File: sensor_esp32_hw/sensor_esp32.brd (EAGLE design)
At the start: 58.5 x 25.5 mm, 31 parts, among them IC1 ESP32-C3-WROOM-02-N4, IC2 ESP32-WROOM-32UE-N16, Q1 DMG3415, U1 AHT20, U2 TPL5110

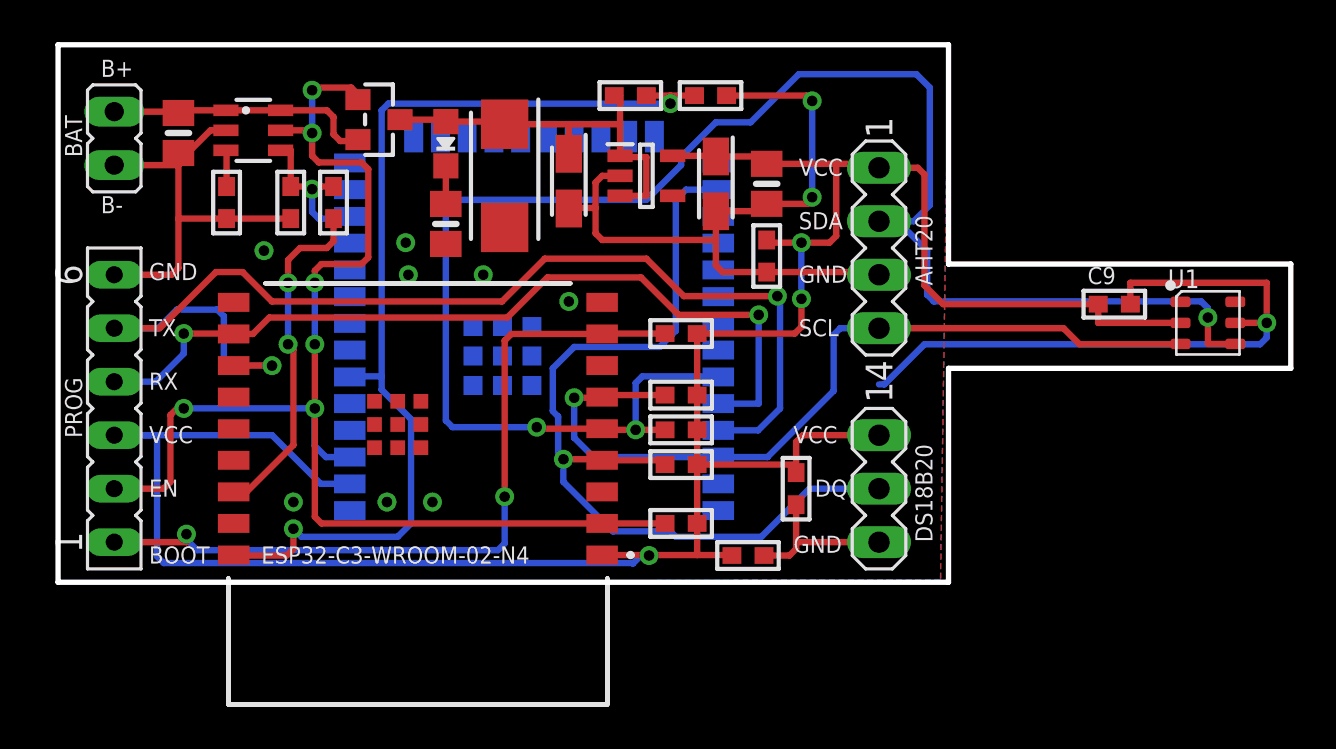
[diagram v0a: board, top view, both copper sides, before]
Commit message: added another esp32 with u.fl connection (if needed)
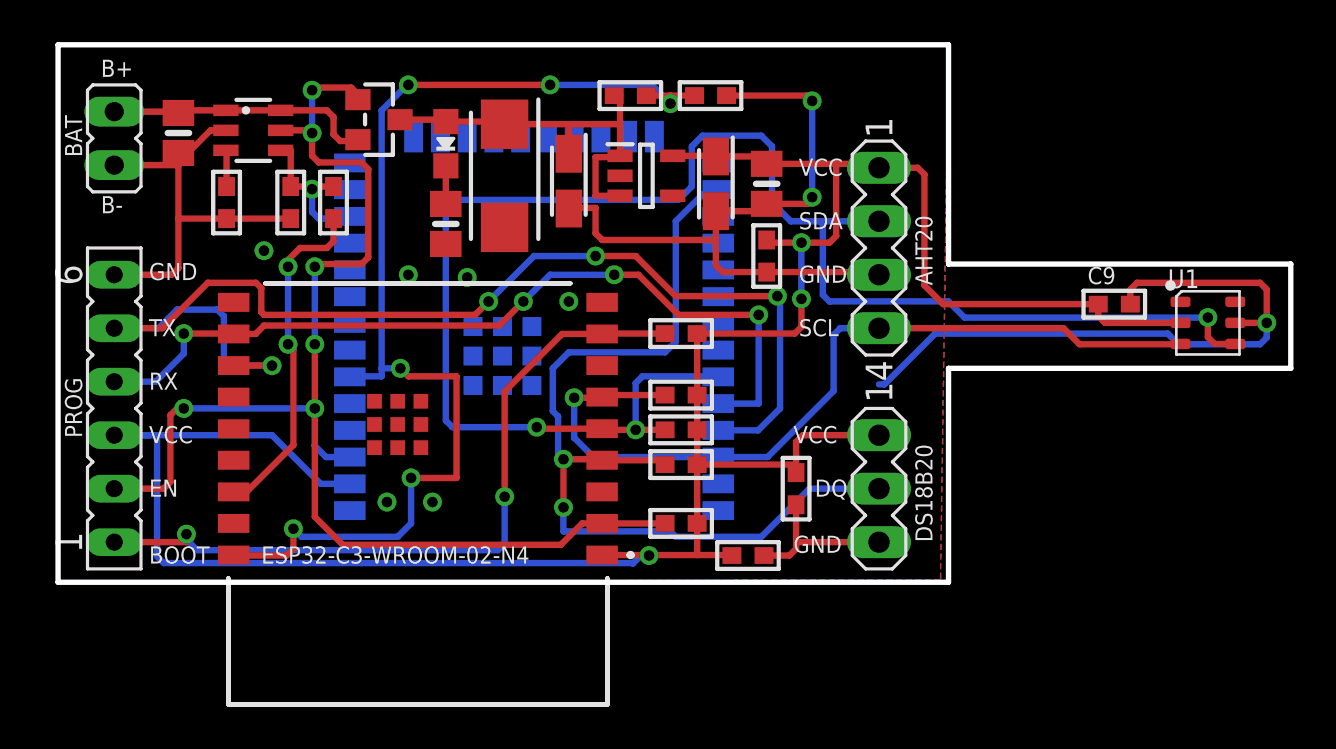
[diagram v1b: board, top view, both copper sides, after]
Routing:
- net PWROUT_DIV: track 48.2 -> 54.2 mm, vias 2 -> 6
- net SDA: track 83.3 -> 79.2 mm
- net GND: track 93.9 -> 91.4 mm, vias 11 -> 9
- net BOOT: track 36.9 -> 35.5 mm
- net EN: track 62.4 -> 63.6 mm
- net DQ: track 42.7 -> 43.8 mm, vias 1 -> 2
- net TXD0: track 55.5 -> 56.4 mm, vias 2 -> 4
- net RXD0: track 40.1 -> 40.2 mm, vias 2 -> 4

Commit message: minor routing improvements
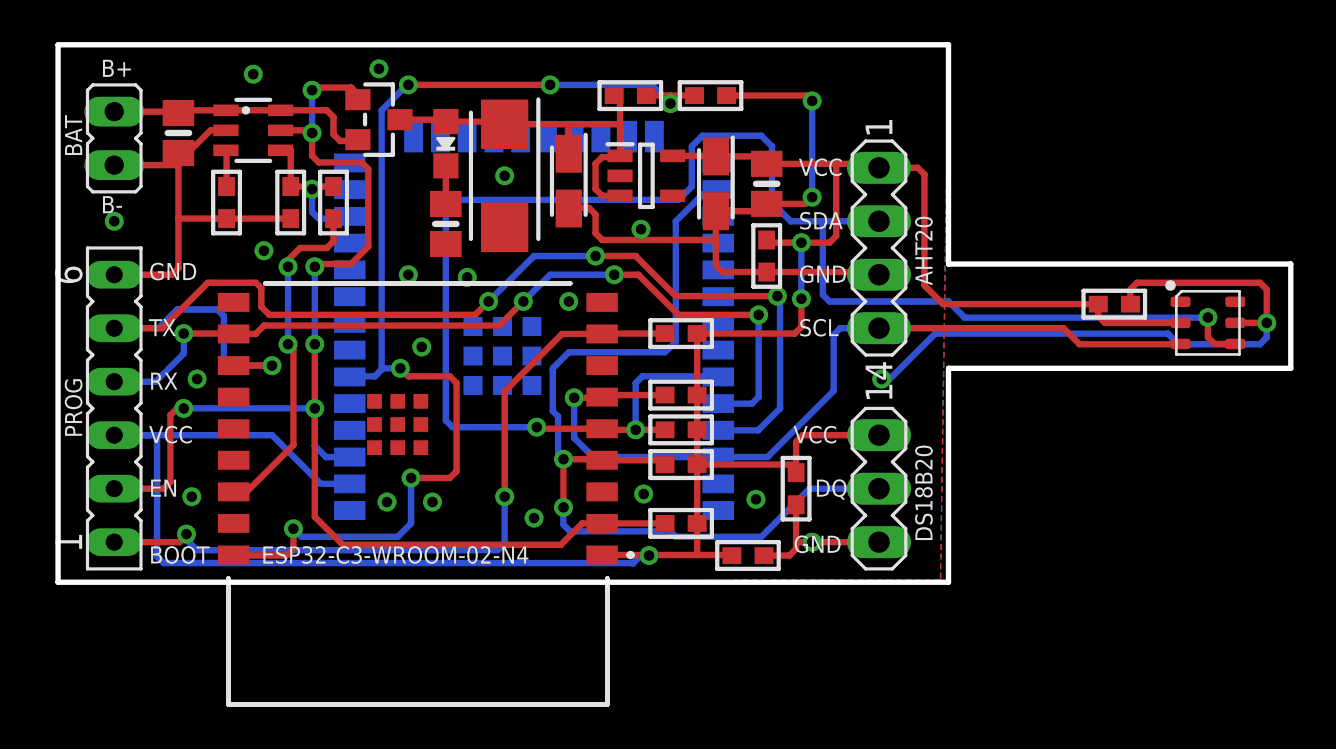
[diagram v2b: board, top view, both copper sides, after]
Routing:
- net PWROUT_DIV: track 54.2 -> 53.7 mm
- net GND: track 91.4 -> 91.1 mm, vias 9 -> 22

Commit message: minor improvements before fabrication
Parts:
- added C10, C11: 100 nF, microbuilder:_0603
- C3: value 22 uF -> 10 uF
- PS1: value AP2202K-3.3TRG1 -> LDI8119-3.3EN-DIO
- moved C2 8.81 mm to (29.5, 18.3)
- moved C4 8.64 mm to (38.6, 22.4), turned to 0 degrees
- moved R11 2.96 mm to (33.4, 22.5)
- moved C3 2.16 mm to (21.6, 18.9)
- moved PS1 2.16 mm to (25.3, 19.2)
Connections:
- net GND: now also C10.2, C11.2
- net N$1: now also IC1.15; no longer IC1.16
- net PWROUT: now also C11.1; no longer C2.1
- net PWROUT_DIV: now also C10.1
- net VCC: now also C2.1
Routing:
- net GND: track 91.1 -> 80.9 mm, vias 22 -> 23
- net VCC: track 117.9 -> 123.5 mm
- net PWROUT_DIV: track 53.7 -> 58.3 mm
- net N$1: track 16.3 -> 15.0 mm
- net TXD0: track 56.2 -> 55.2 mm
- net PWROUT: track 19.1 -> 20.1 mm

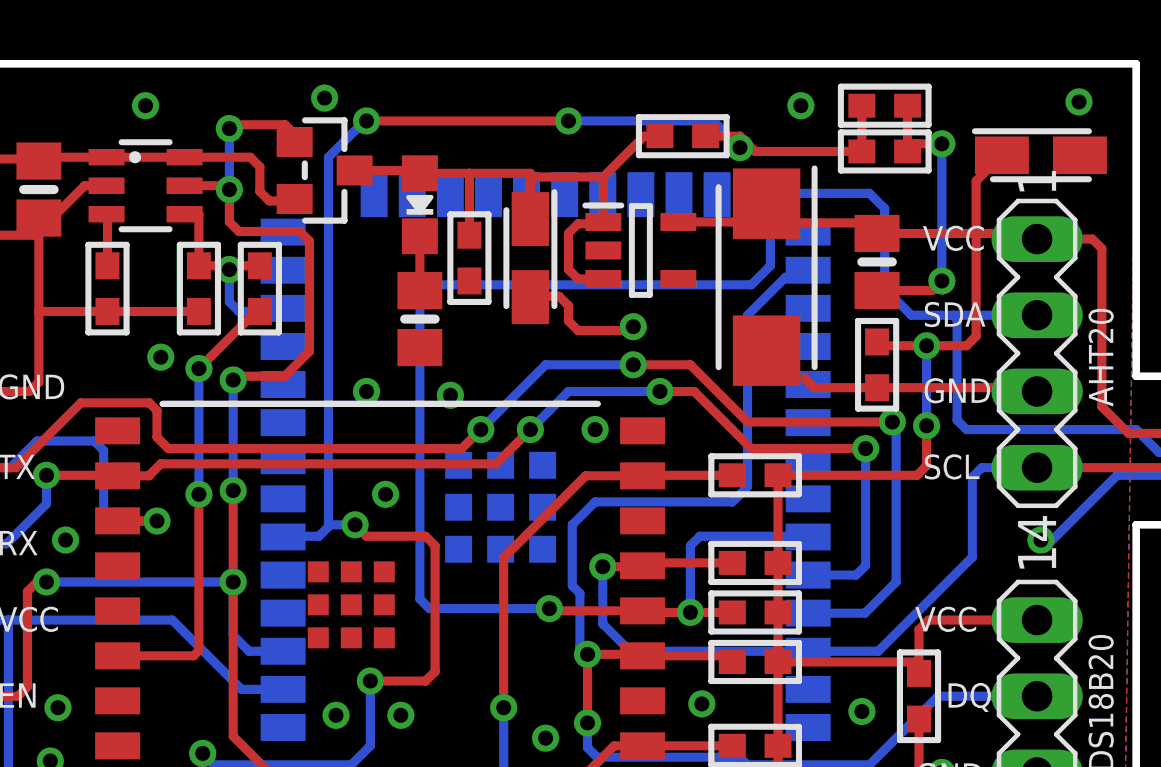
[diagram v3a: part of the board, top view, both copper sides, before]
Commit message: fixes to schematic and pcb, also made esp32 sensor work
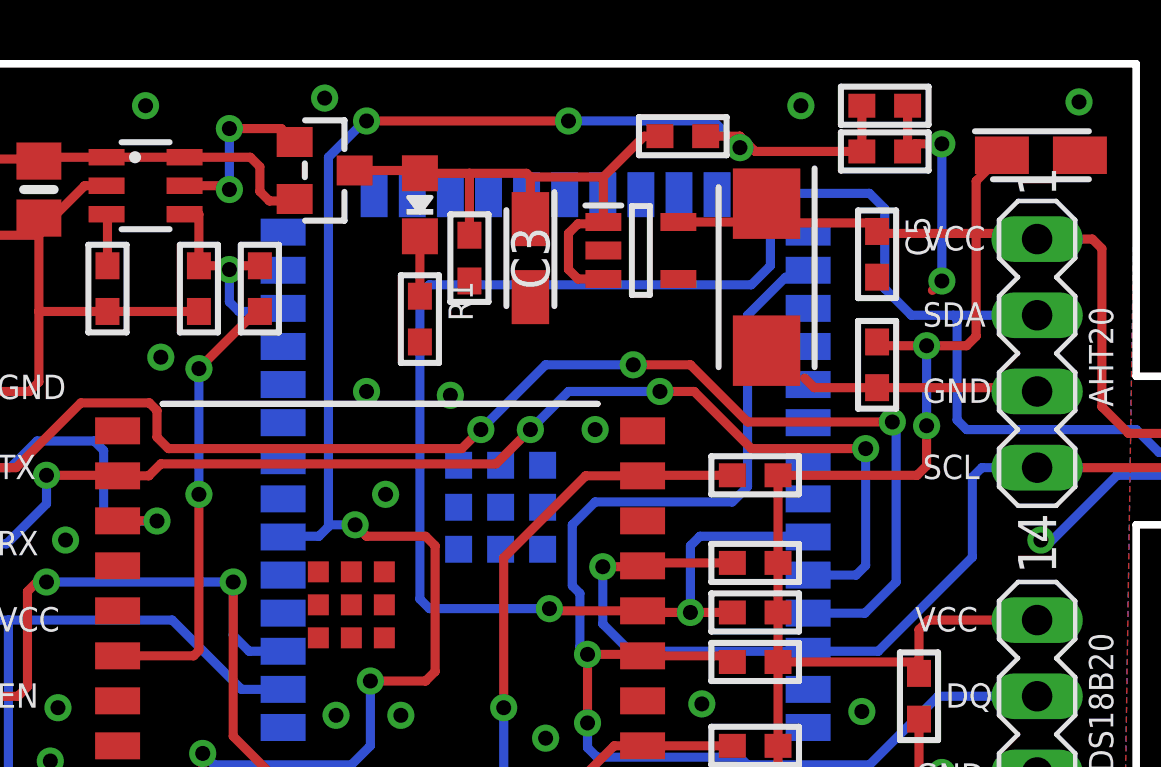
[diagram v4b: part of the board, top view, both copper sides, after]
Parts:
- C3: value 10 uF -> 22 uF
- C5: device microbuilder:0805-NO -> microbuilder:_0603
- R1: value 1K -> 1k; device microbuilder:0805-NO -> microbuilder:_0603
- moved C5 0.25 mm to (33.1, 19.1)
- turned R1 to 270 degrees
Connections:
- new net DRVN: Q1.1, U2.5
- net EN: no longer Q1.1, U2.5
- net GND: now also R1.2; no longer R1.1
- net N$3: now also R1.1; no longer R1.2
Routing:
- net EN: track 63.3 -> 39.4 mm, vias 6 -> 2
- net GND: track 80.9 -> 74.3 mm, vias 23 -> 22
- net DRVN: track 0.00 -> 6.01 mm, vias 0 -> 2

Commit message: added pull up on BOOT1 for flashing via serial
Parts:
- added R12: 10k, microbuilder:_0603
- moved R8 0.13 mm to (29.1, 8.64)
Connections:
- net BOOT1: now also R12.1
- net VCC: now also R12.2
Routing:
- net BOOT1: track 0.00 -> 3.00 mm
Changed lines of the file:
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@@
 <setting verticaltext="up"/>
 </settings>
-<grid distance="0.005" unitdist="inch" unit="mm" style="dots" multiple="1" display="yes" altdistance="0.025" altunitdist="inch" altunit="mm"/>
+<grid distance="0.0635" unitdist="mm" unit="mm" style="dots" multiple="1" display="yes" altdistance="0.025" altunitdist="inch" altunit="mm"/>
 <layers>
 <layer number="1" name="Top" color="4" fill="1" visible="yes" active="yes"/>
@@
 <element name="C7" library="microbuilder" package="_0603" value="100 nF" x="33.147" y="15.367" smashed="yes" rot="R270"/>
 <element name="R7" library="microbuilder" package="_0603" value="1k" x="12.573" y="17.907" smashed="yes" rot="R270"/>
-<element name="R8" library="microbuilder" package="_0603" value="4k7" x="29.083" y="8.763" smashed="yes"/>
+<element name="R8" library="microbuilder" package="_0603" value="4k7" x="29.083" y="8.636" smashed="yes"/>
 <element name="R9" library="microbuilder" package="_0603" value="4k7" x="29.083" y="7.112" smashed="yes"/>
 <element name="R10" library="microbuilder" package="_0603" value="10k" x="26.67" y="22.987" smashed="yes" rot="R180"/>
@@
 <attribute name="TME_ELECTRONIC_COMPONENTS_PRICE-STOCK" value="" x="21.59" y="18.923" size="1.778" layer="27" rot="R270" display="off"/>
 </element>
+<element name="R12" library="microbuilder" package="_0603" value="10k" x="29.083" y="10.16"/>
 </elements>
 <signals>
@@
 <wire x1="36.1315" y1="16.002" x2="36.449" y2="16.3195" width="0.3048" layer="1"/>
 <wire x1="36.449" y1="16.3195" x2="36.449" y2="19.746" width="0.3048" layer="1"/>
-<wire x1="29.845" y1="11.684" x2="29.845" y2="8.763" width="0.3048" layer="1"/>
-<wire x1="29.845" y1="8.763" x2="29.845" y2="7.112" width="0.3048" layer="1"/>
+<wire x1="29.845" y1="11.684" x2="29.845" y2="10.16" width="0.3048" layer="1"/>
+<wire x1="29.845" y1="10.0965" x2="29.845" y2="8.636" width="0.3048" layer="1"/>
+<wire x1="29.845" y1="8.636" x2="29.845" y2="7.112" width="0.3048" layer="1"/>
 <wire x1="29.845" y1="7.112" x2="29.845" y2="5.461" width="0.3048" layer="1"/>
 <wire x1="29.845" y1="5.461" x2="29.845" y2="2.667" width="0.3048" layer="1"/>
@@
 <wire x1="33.213" y1="19.746" x2="33.147" y2="19.812" width="0.3048" layer="1"/>
 <wire x1="33.147" y1="20.096" x2="33.147" y2="19.812" width="0.3048" layer="1"/>
+<contactref element="R12" pad="2"/>
+<wire x1="29.845" y1="10.16" x2="29.845" y2="10.0965" width="0.3048" layer="1"/>
 </signal>
 <signal name="BOOT1">
 <contactref element="IC1" pad="7"/>
+<contactref element="R12" pad="1"/>
+<wire x1="28.321" y1="10.16" x2="25.331" y2="10.16" width="0.3048" layer="1"/>
+<wire x1="25.331" y1="10.16" x2="25.331" y2="10.166" width="0.3048" layer="1"/>
 </signal>
 <signal name="DQ">
@@
 <contactref element="IC1" pad="6"/>
 <contactref element="R8" pad="1"/>
-<wire x1="28.321" y1="8.763" x2="25.331" y2="8.763" width="0.3048" layer="1"/>
 <wire x1="25.331" y1="8.763" x2="25.331" y2="8.666" width="0.3048" layer="1"/>
 <via x="24.003" y="8.636" extent="1-16" drill="0.5"/>
 <wire x1="24.003" y1="8.636" x2="25.331" y2="8.636" width="0.3048" layer="1"/>
-<wire x1="25.331" y1="8.636" x2="25.331" y2="8.666" width="0.3048" layer="1"/>
 <wire x1="38.481" y1="11.938" x2="36.6395" y2="11.938" width="0.3048" layer="16"/>
 <wire x1="36.6395" y1="11.938" x2="36.322" y2="11.6205" width="0.3048" layer="16"/>
@@
 <wire x1="24.916" y1="5.818" x2="24.003" y2="6.731" width="0.3048" layer="16"/>
 <wire x1="24.003" y1="6.731" x2="24.003" y2="8.636" width="0.3048" layer="16"/>
+<wire x1="28.321" y1="8.636" x2="25.331" y2="8.636" width="0.3048" layer="1"/>
+<wire x1="25.331" y1="8.636" x2="25.331" y2="8.666" width="0.3048" layer="1"/>
 </signal>
 <signal name="PWROUT_DIV">
